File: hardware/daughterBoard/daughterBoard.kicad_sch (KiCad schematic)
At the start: 31 parts

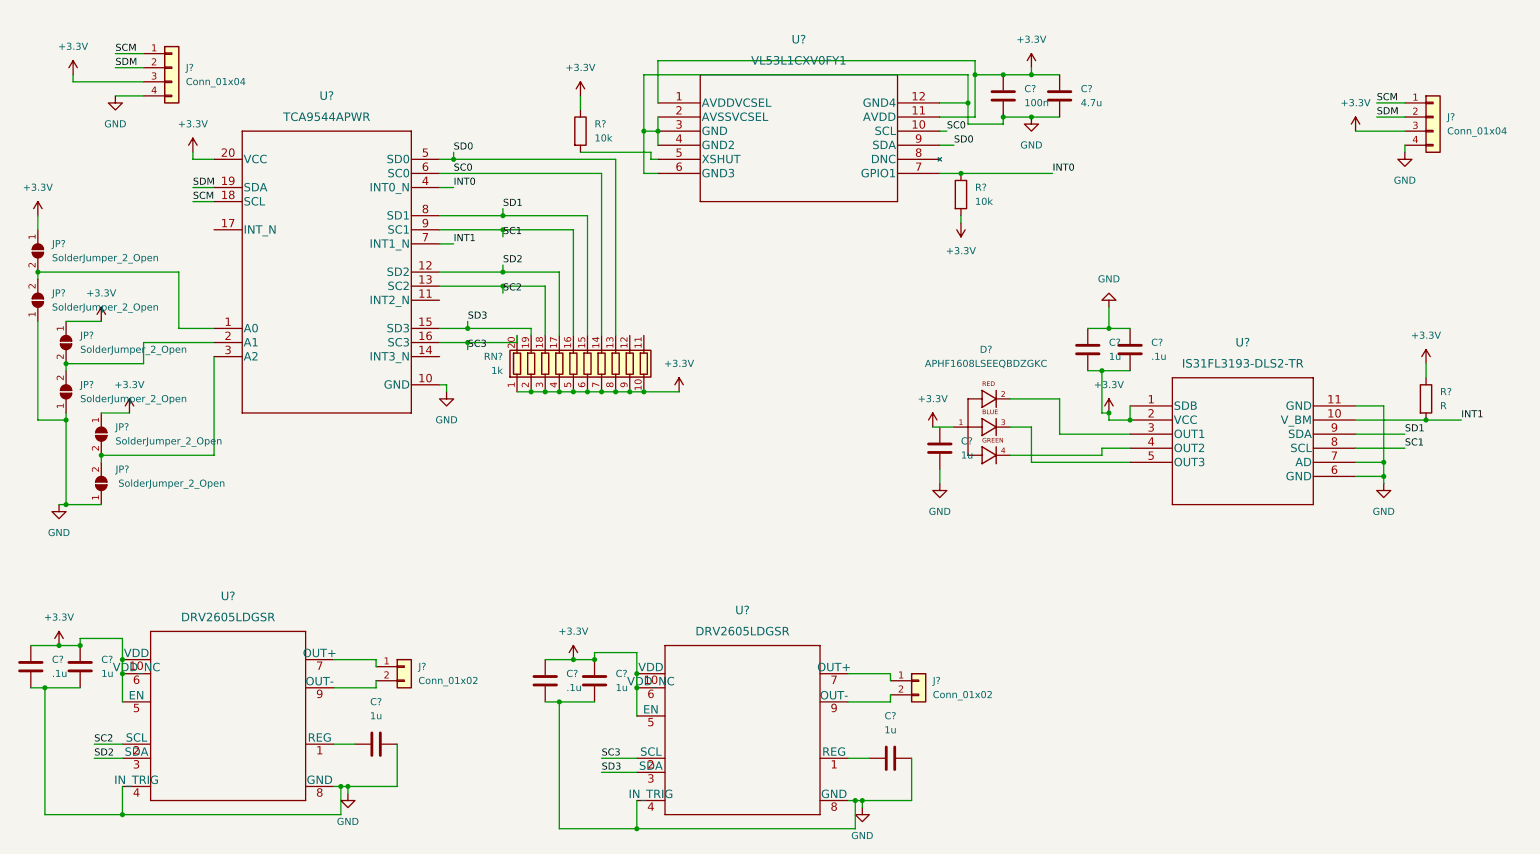
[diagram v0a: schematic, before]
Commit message: edit connectors, finish annotating schematic, use all discrete resistors, assign footprints, get general board layout set
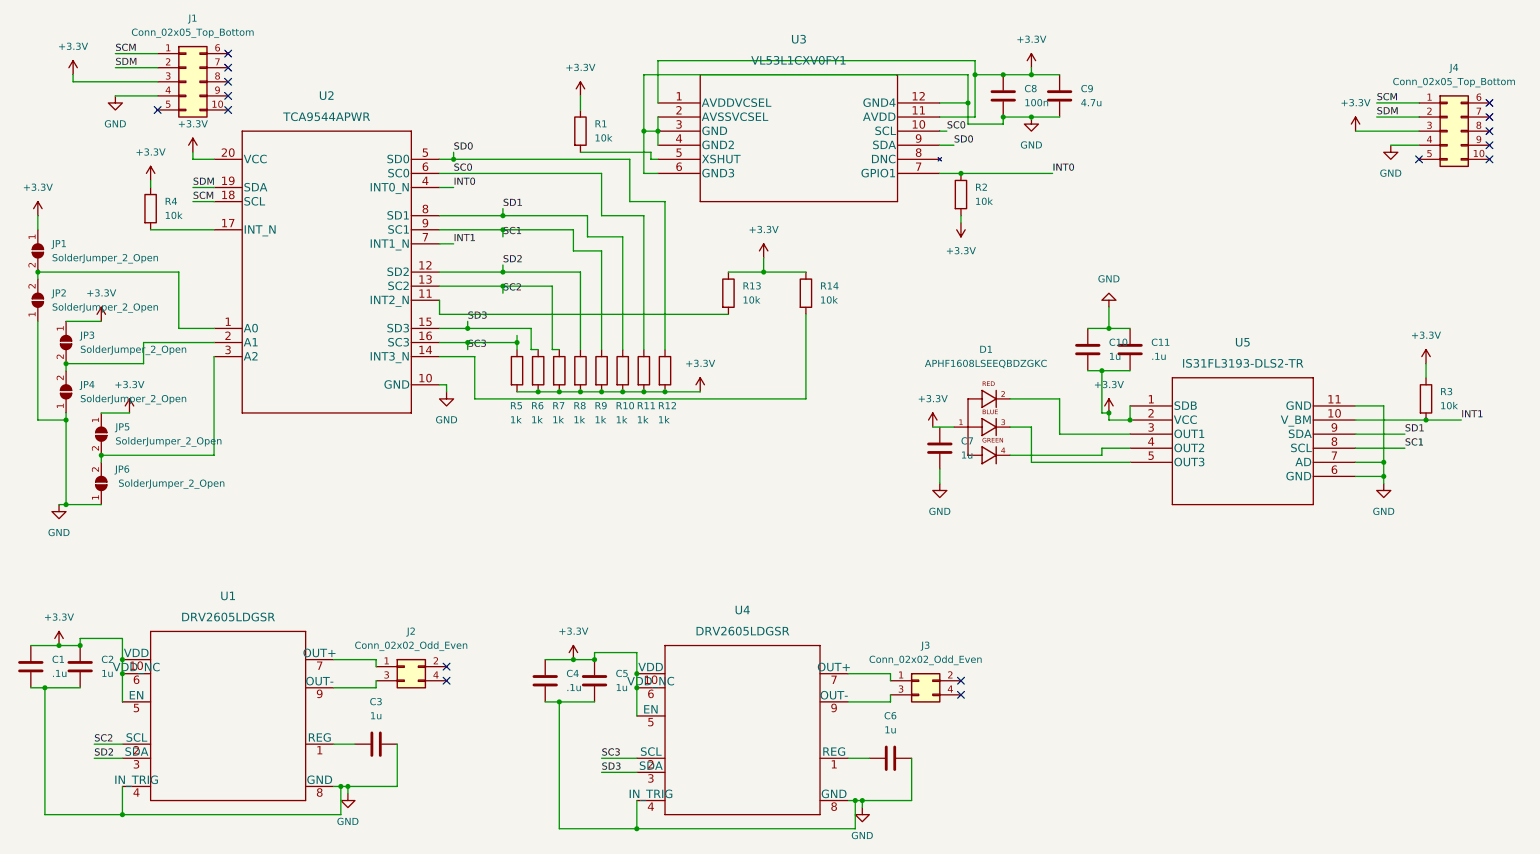
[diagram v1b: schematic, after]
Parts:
- removed J? (x2): Conn_01x04, symbol Connector_Generic:Conn_01x04
- removed J? (x2): Conn_01x02, symbol Connector_Generic:Conn_01x02
- removed RN?: 1k, symbol Device:R_Pack10
- added J1, J4: Conn_02x05_Top_Bottom, Connector_PinHeader_2.54mm:PinHeader_2x05_P2.54mm_Vertical, symbol Connector_Generic:Conn_02x05_Top_Bottom
- added J2, J3: Conn_02x02_Odd_Even, Connector_PinHeader_2.54mm:PinHeader_2x02_P2.54mm_Vertical, symbol Connector_Generic:Conn_02x02_Odd_Even
- added R10, R11, R12, R5, R6, R7, R8, R9: 1k, Resistor_SMD:R_0603_1608Metric_Pad0.98x0.95mm_HandSolder, symbol Device:R
- added R13, R14, R4: 10k, Resistor_SMD:R_0603_1608Metric_Pad0.98x0.95mm_HandSolder, symbol Device:R
- C1, C10, C11, C2, C3, C4, C5, C6, C7, C8, C9: renamed from C?; footprint (none) -> Capacitor_SMD:C_0805_2012Metric_Pad1.18x1.45mm_HandSolder
- D1: renamed from D?; footprint LED_APHF1608LSEEQBDZGKC -> LED:LED_APHF1608LSEEQBDZGKC
- JP1, JP2, JP3, JP4, JP5, JP6: renamed from JP?; footprint (none) -> Jumper:SolderJumper-2_P1.3mm_Open_TrianglePad1.0x1.5mm
- R1, R2: renamed from R?; footprint (none) -> Resistor_SMD:R_0603_1608Metric_Pad0.98x0.95mm_HandSolder
- R3: renamed from R?; value R -> 10k; footprint (none) -> Resistor_SMD:R_0603_1608Metric_Pad0.98x0.95mm_HandSolder
- U1, U4: renamed from U?; footprint DGS0010A -> MotorDriver:DRV2605LDGSR
- U2: renamed from U?; footprint PW0020A_N -> I2CMultiplexor:TCA9544APWR
- U3: renamed from U?; footprint LGA12_STM -> TOF:VL53L1CXV0FY&slash_1
- U5: renamed from U?; footprint DFN-10_ISI -> LEDDriver:IS31FL3193-DLS2-TR
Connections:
- net +3V3: now also J1.3 (Pin_3), J4.3 (Pin_3), R10.2, R11.2, R12.2, R13.1, R14.1, R4.1, R5.2, R6.2, R7.2, R8.2, R9.2
- net GND: now also J1.4 (Pin_4), J4.4 (Pin_4)
- net SC0: now also R11.1
- net SC1: now also R9.1
- net SC2: now also R7.1
- net SC3: now also R5.1
- net SCM: now also J1.1 (Pin_1), J4.1 (Pin_1)
- net SD0: now also R12.1
- net SD1: now also R10.1
- net SD2: now also R8.1
- net SD3: now also R6.1
- net SDM: now also J1.2 (Pin_2), J4.2 (Pin_2)
- net at U2.11 (INT2_N): now also R13.2
- net at U2.14 (INT3_N): now also R14.2
- net at U2.17 (INT_N): now also R4.2
- net at U4.7 (OUT+): now also J3.1 (Pin_1)
- net at U4.9 (OUT-): now also J3.3 (Pin_3)
- net at U1.7 (OUT+): now also J2.1 (Pin_1)
- net at U1.9 (OUT-): now also J2.3 (Pin_3)
- no-connect marks 0 -> 16

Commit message: v1 finished
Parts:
- removed J1, J4: Conn_02x05_Top_Bottom, Connector_PinHeader_2.54mm:PinHeader_2x05_P2.54mm_Vertical, symbol Connector_Generic:Conn_02x05_Top_Bottom
- added C12: .1u, Capacitor_SMD:C_0805_2012Metric_Pad1.18x1.45mm_HandSolder, symbol Device:C
- added C13: 1u, Capacitor_SMD:C_0805_2012Metric_Pad1.18x1.45mm_HandSolder, symbol Device:C
- added J1, J4: Conn_02x05_Odd_Even, Connector_PinHeader_2.54mm:PinHeader_2x05_P2.54mm_Vertical, symbol Connector_Generic:Conn_02x05_Odd_Even
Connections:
- net +3V3: now also C7.1, R2.1, C12.1, C13.1, J1.5 (Pin_5), J1.6 (Pin_6), J4.5 (Pin_5), J4.6 (Pin_6); no longer R2.2
- net GND: now also C12.2, C13.2, J1.7 (Pin_7), J1.8 (Pin_8), J4.7 (Pin_7), J4.8 (Pin_8)
- net INT0: now also R2.2; no longer R2.1, U3.7 (GPIO1)
- net INT1: now also U3.7 (GPIO1); no longer U5.10 (V_BM)
- net SC0: now also U4.2 (SCL); no longer U3.10 (SCL)
- net SC1: now also U3.10 (SCL); no longer U5.8 (SCL)
- net SC2: now also U5.8 (SCL); no longer U1.2 (SCL)
- net SC3: now also U1.2 (SCL); no longer U4.2 (SCL)
- net SCM: now also J1.1 (Pin_1), J4.1 (Pin_1)
- net SD0: now also U4.3 (SDA); no longer U3.9 (SDA)
- net SD1: now also U3.9 (SDA); no longer U5.9 (SDA)
- net SD2: now also U5.9 (SDA); no longer U1.3 (SDA)
- net SD3: now also U1.3 (SDA); no longer U4.3 (SDA)
- net SDM: now also J1.3 (Pin_3), J4.3 (Pin_3)
- net INT2: now reaches R13.2, U2.11 (INT2_N)
- net INT2: now also U5.10 (V_BM)
- net INT3: now reaches R14.2, U2.14 (INT3_N)
- no-connect marks 16 -> 12

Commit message: updated board files to rev2
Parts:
- removed D1: APHF1608LSEEQBDZGKC, LED:LED_APHF1608LSEEQBDZGKC, symbol LED:APHF1608LSEEQBDZGKC
- added LED1: LEDRGB, LED_New:150352M173300, symbol LED_New:LEDRGB
- C1, C10, C11, C12, C13, C2, C3, C4, C5, C6, C7, C9: footprint Capacitor_SMD:C_0805_2012Metric_Pad1.18x1.45mm_HandSolder -> Capacitor_SMD:C_01005_0402Metric_Pad0.57x0.30mm_HandSolder
- C8: value 100n -> .1u; footprint Capacitor_SMD:C_0805_2012Metric_Pad1.18x1.45mm_HandSolder -> Capacitor_SMD:C_01005_0402Metric_Pad0.57x0.30mm_HandSolder
- J1, J4: footprint Connector_PinHeader_2.54mm:PinHeader_2x05_P2.54mm_Vertical -> Connector_PinHeader_1.27mm:PinHeader_2x05_P1.27mm_Vertical
- R1, R10, R11, R12, R13, R14, R2, R3, R4, R5, R6, R7, R8, R9: footprint Resistor_SMD:R_0603_1608Metric_Pad0.98x0.95mm_HandSolder -> Resistor_SMD:R_01005_0402Metric_Pad0.57x0.30mm_HandSolder
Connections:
- net +3V3: now also LED1.2, LED1.4, LED1.6
- net at U5.3 (OUT1): now also LED1.3
- net at U5.5 (OUT3): now also LED1.1
- net at U5.4 (OUT2): now also LED1.5
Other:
- moved on the sheet: C7
